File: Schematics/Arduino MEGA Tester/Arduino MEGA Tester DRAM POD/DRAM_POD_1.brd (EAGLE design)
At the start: 57.1 x 76.2 mm, 9 parts

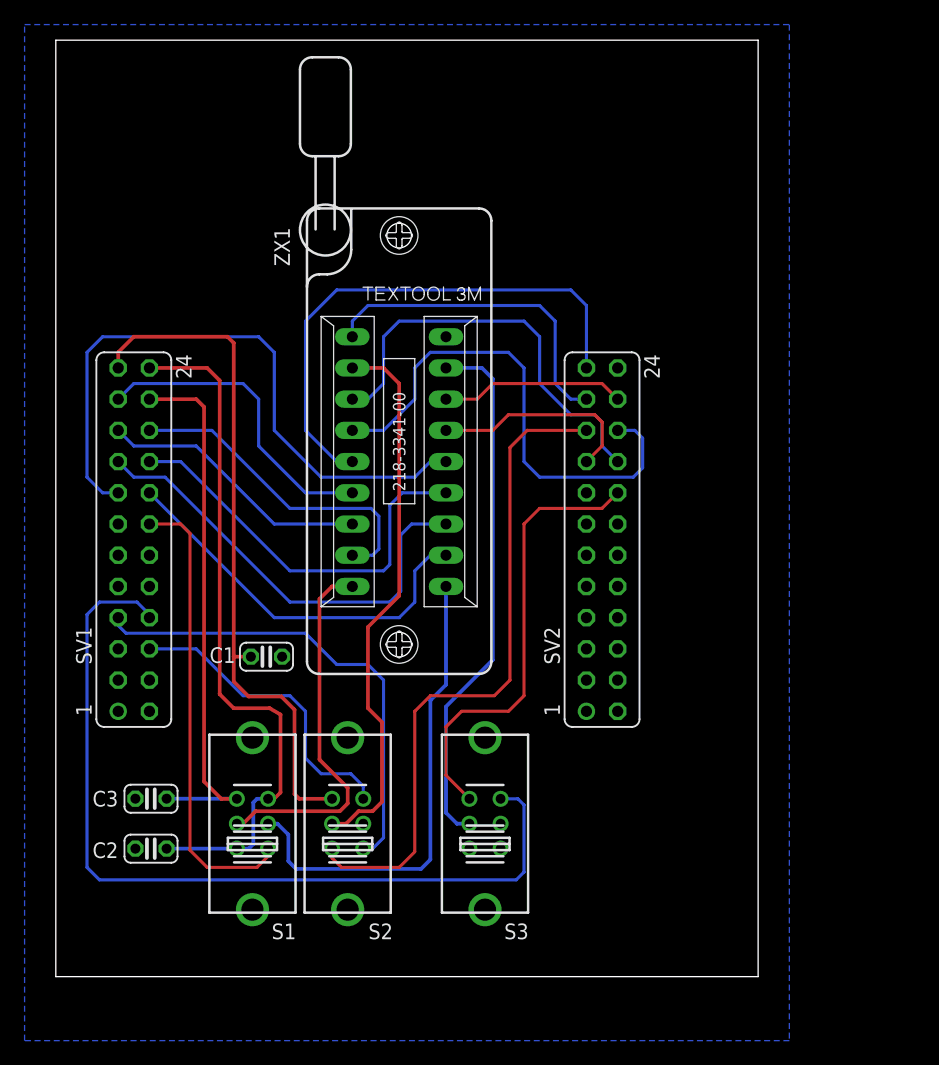
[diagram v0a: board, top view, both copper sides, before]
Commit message: Moved a few I/O around. Added some pin mapping files. Adjusted OLED position.
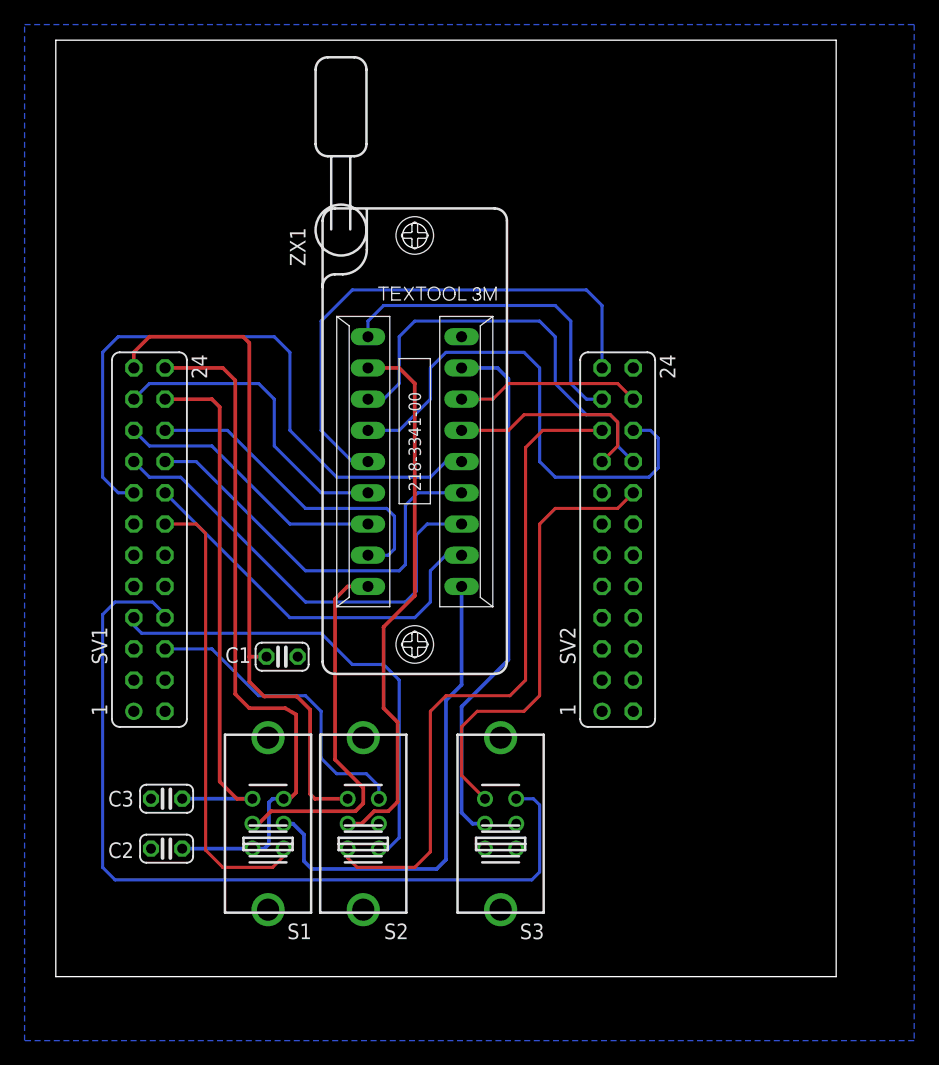
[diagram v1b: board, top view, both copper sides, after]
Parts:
- moved S3 1.27 mm to (36.2, 12.4)
- moved SV1 1.27 mm to (7.62, 35.6)
- moved C1 1.27 mm to (18.4, 26.0)
- moved C2 1.27 mm to (9.02, 10.4)
- moved C3 1.27 mm to (9.02, 14.5)
- moved S1 1.27 mm to (17.3, 12.4)
- moved S2 1.27 mm to (25.0, 12.4)
- moved ZX1 1.27 mm to (29.2, 41.9)
- moved SV2 1.27 mm to (45.7, 35.6)
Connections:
- removed net AB0: SV1.5
- removed net AB1: SV1.4
- removed net AB2: SV1.3
- new net CA0X: SV2.14
- new net CA1X: SV2.13
- new net CA3X: SV2.12
- new net CA4X: SV2.11
- net CB0: now also SV1.5; no longer SV2.14
- net CB1: now also SV1.4; no longer SV2.13
- net CB2: now also SV1.3; no longer SV2.12
- net CB3: now also SV1.2; no longer SV2.11
- net GND: no longer SV1.2
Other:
- board size 57.1 x 76.2 mm -> 63.5 x 76.2 mm
